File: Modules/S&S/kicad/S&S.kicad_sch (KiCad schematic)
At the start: 59 parts, among them Q1 BC547, Q2 J112, U1 TL074, U2 TL074

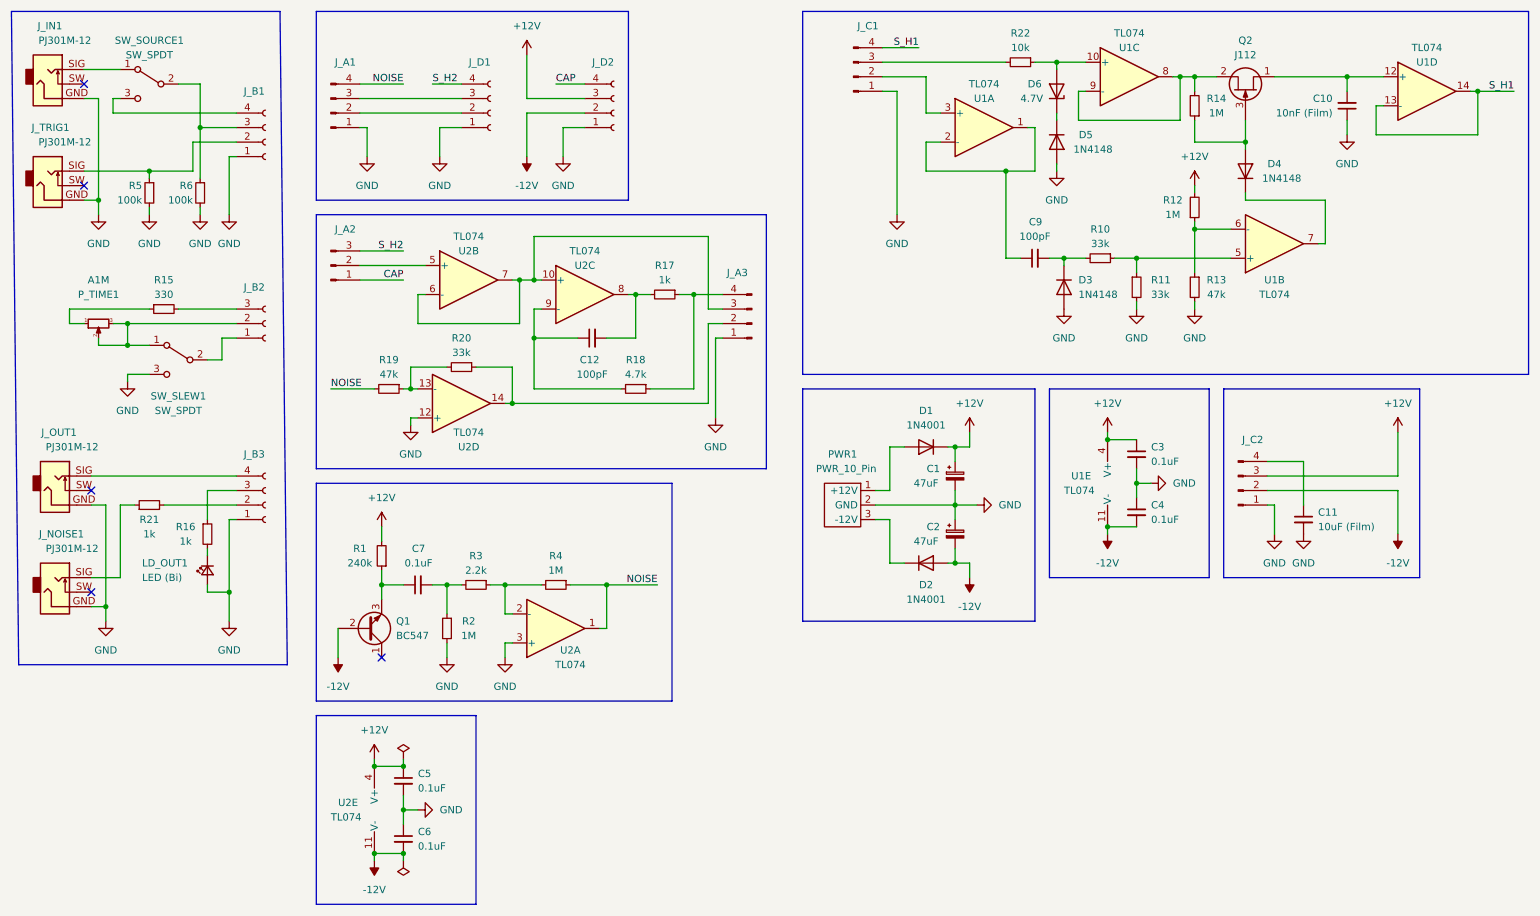
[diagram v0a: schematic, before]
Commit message: Update S&S for KiCad 8, update capacitor size and BOM.
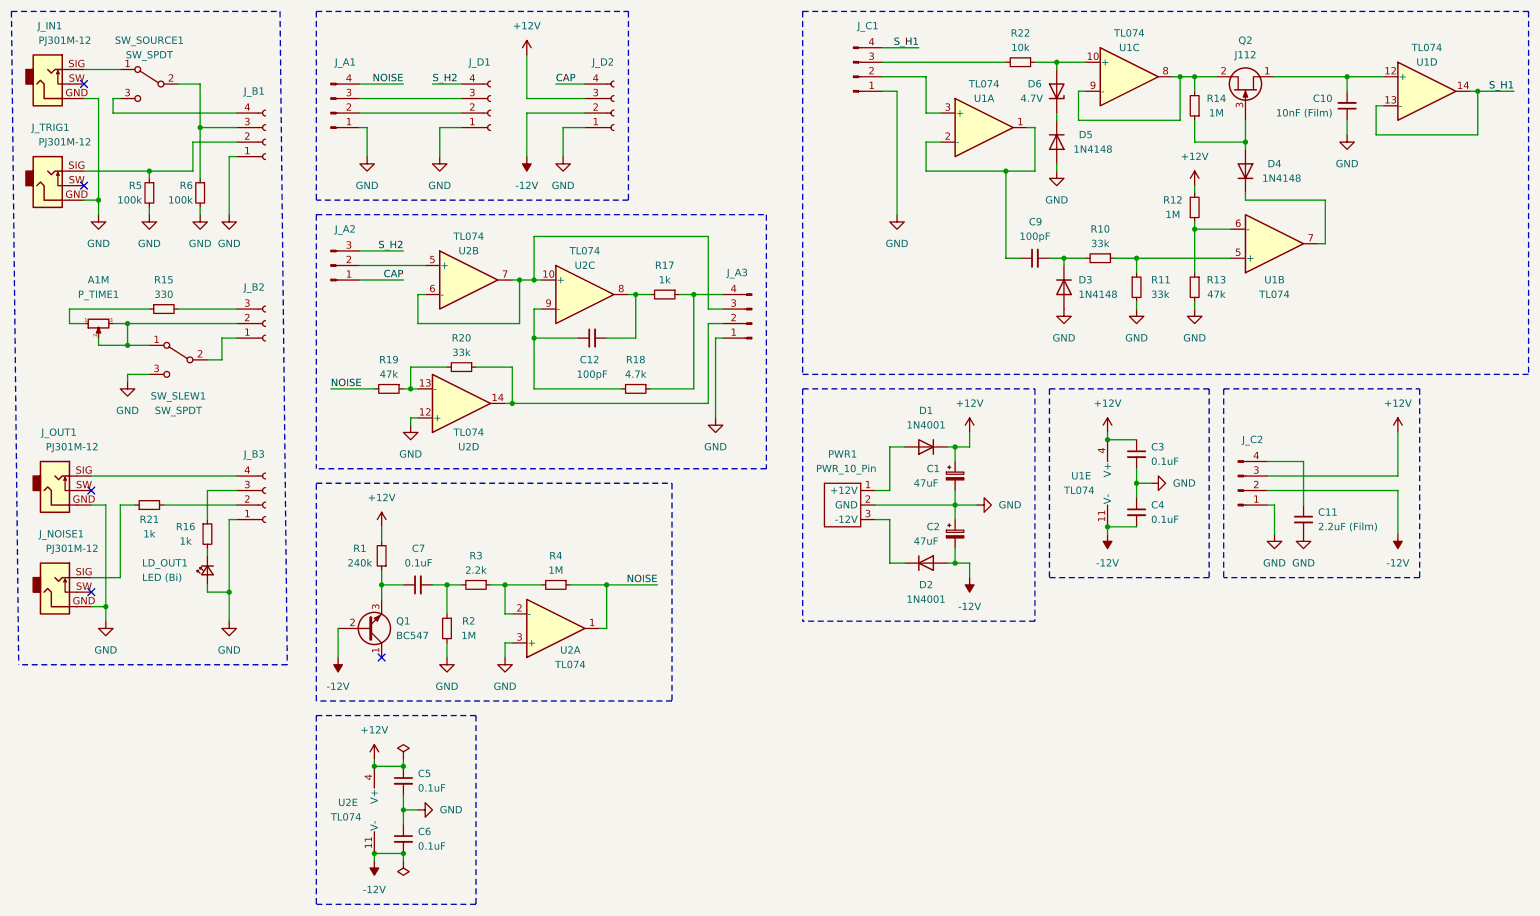
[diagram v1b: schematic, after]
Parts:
- C11: value 10uF (Film) -> 2.2uF (Film)
- LD_OUT1: Spice_Lib_File /home/ebu/Documents/KiCad/KiCad-Spice-Library/Models/Diode/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 -> (none); Spice_Model LED_GENERAL -> (none); Spice_Netlist_Enabled Y -> (none); Spice_Primitive D -> (none)
